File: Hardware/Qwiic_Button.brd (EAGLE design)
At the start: 25.4 x 25.4 mm, 48 parts, among them J2 QWIIC_RIGHT_ANGLE, J3 QWIIC_RIGHT_ANGLE, J7 ISP, U4 ATTINY84-ARDUINO

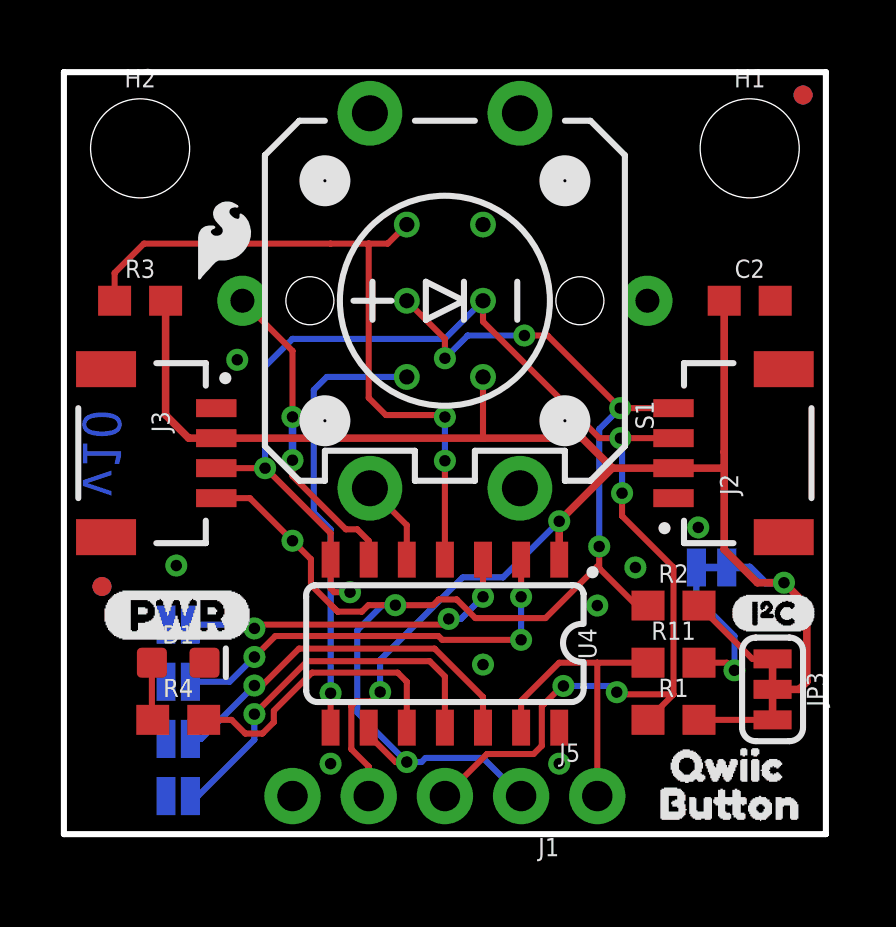
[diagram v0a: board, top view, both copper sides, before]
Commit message: adding polarity marker to button
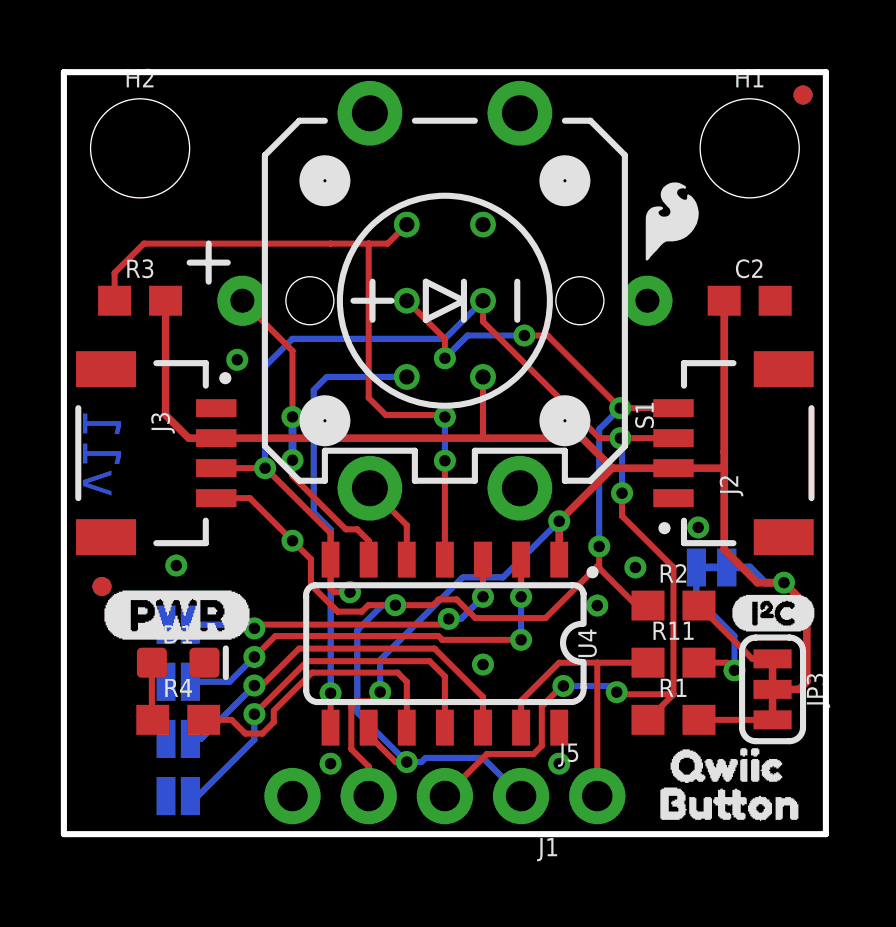
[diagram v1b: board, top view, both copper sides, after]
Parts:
- moved LOGO4 14.9 mm to (20.3, 20.4)
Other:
- board text added: "v11"
- board text removed: "v10"
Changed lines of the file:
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@@
 <?xml version="1.0" encoding="utf-8"?>
 <!DOCTYPE eagle SYSTEM "eagle.dtd">
-<eagle version="9.1.0">
+<eagle version="9.5.2">
 <drawing>
 <settings>
@@
 <wire x1="25.4" y1="25.4" x2="0" y2="25.4" width="0.2032" layer="20"/>
 <wire x1="0" y1="25.4" x2="0" y2="0" width="0.2032" layer="20"/>
-<text x="1.27" y="12.7" size="1.27" layer="16" font="vector" ratio="15" rot="SMR90" align="center">v10</text>
+<text x="1.27" y="12.7" size="1.27" layer="16" font="vector" ratio="15" rot="SMR90" align="center">v11</text>
 <text x="11.43" y="-8.89" size="1.778" layer="51" font="vector">Fisher M.</text>
 <text x="10.16" y="-11.43" size="1.778" layer="51" font="vector">Andy England</text>
@@
 <element name="U$19" library="buzzard_labels (8)" package="A22" value="" x="3.683" y="3.175" smashed="yes" rot="MR0"/>
 <element name="U$21" library="buzzard_labels (8)" package="A33" value="" x="3.4925" y="1.27" smashed="yes" rot="MR0"/>
-<element name="LOGO2" library="SparkFun-Aesthetics" package="REVISION" value="REVISION" x="-7.62" y="-11.43"/>
-<element name="LOGO3" library="SparkFun-Aesthetics" package="SFE_LOGO_NAME_.1" value="SFE_LOGO_NAME.1_INCH" x="12.7635" y="21.209" rot="MR0"/>
-<element name="LOGO4" library="SparkFun-Aesthetics" package="SFE_LOGO_FLAME_.1" value="SFE_LOGO_FLAME.1_INCH" x="5.334" y="19.812"/>
+<element name="LOGO2" library="SparkFun-Aesthetics" package="REVISION" value="REVISION" x="-7.62" y="-11.43" smashed="yes"/>
+<element name="LOGO3" library="SparkFun-Aesthetics" package="SFE_LOGO_NAME_.1" value="SFE_LOGO_NAME.1_INCH" x="12.7635" y="21.209" smashed="yes" rot="MR0"/>
+<element name="LOGO4" library="SparkFun-Aesthetics" package="SFE_LOGO_FLAME_.1" value="SFE_LOGO_FLAME.1_INCH" x="20.2565" y="20.447" smashed="yes"/>
 </elements>
 <signals>
